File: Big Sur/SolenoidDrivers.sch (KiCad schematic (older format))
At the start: 32 parts, among them U1 DRV103H, U2 DRV103H, U3 DRV8806

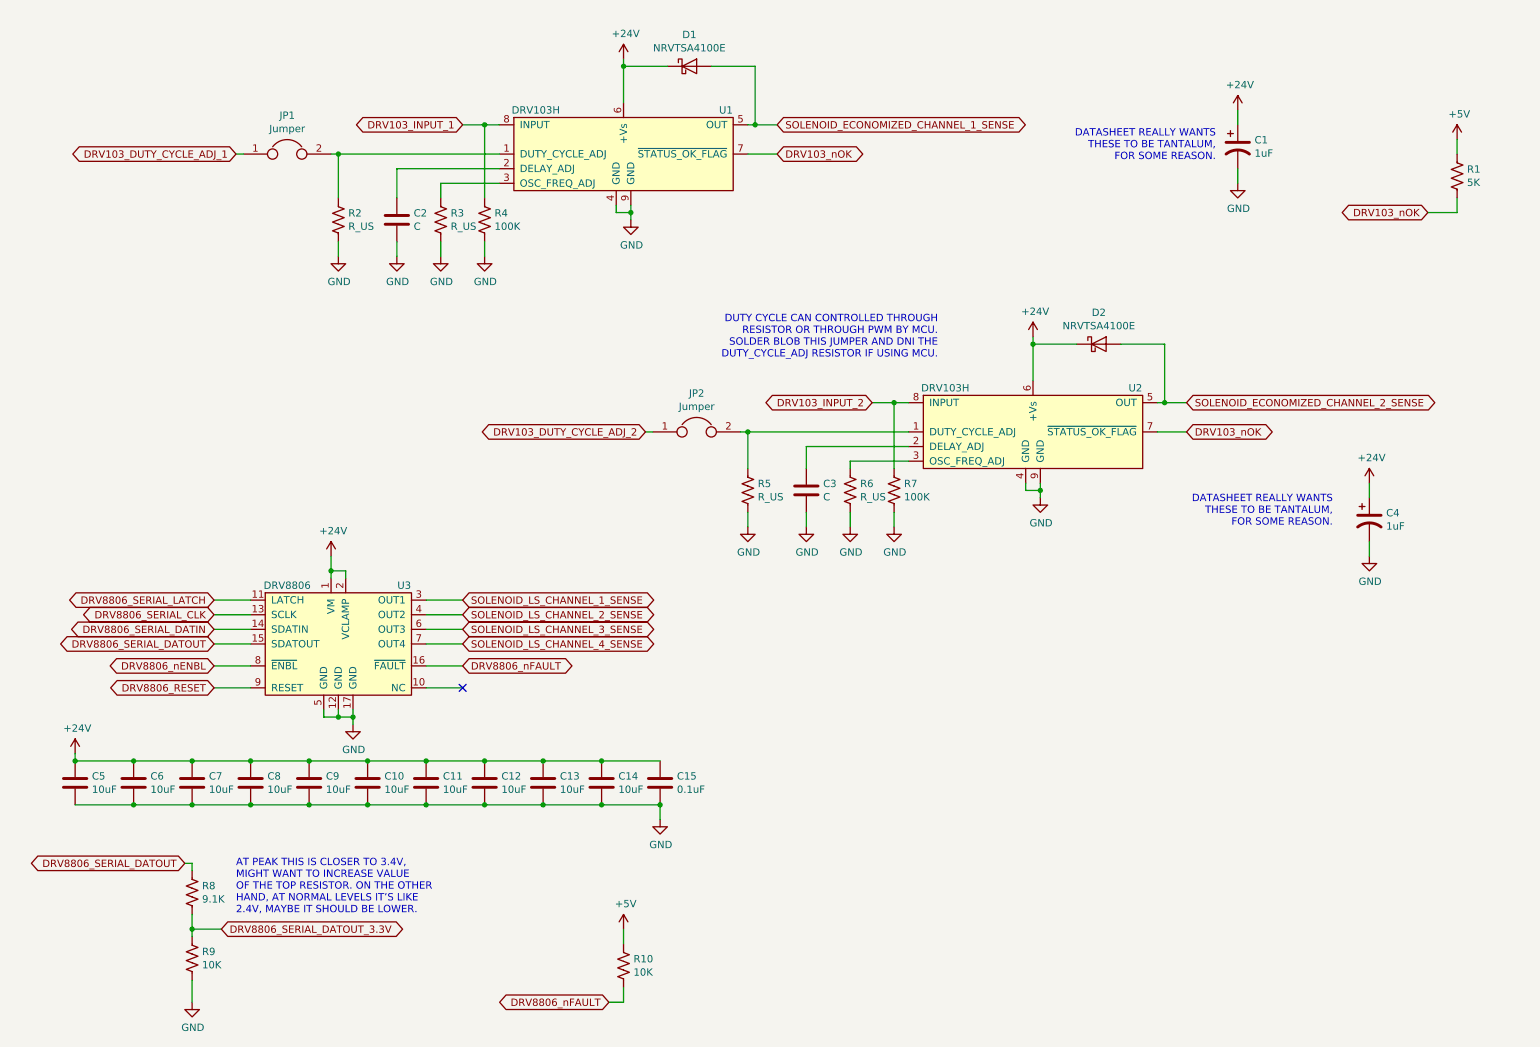
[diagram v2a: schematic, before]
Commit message: Schematics Complete
Still need to spec resistors, and XT30s, then should be ready for layout and routing.
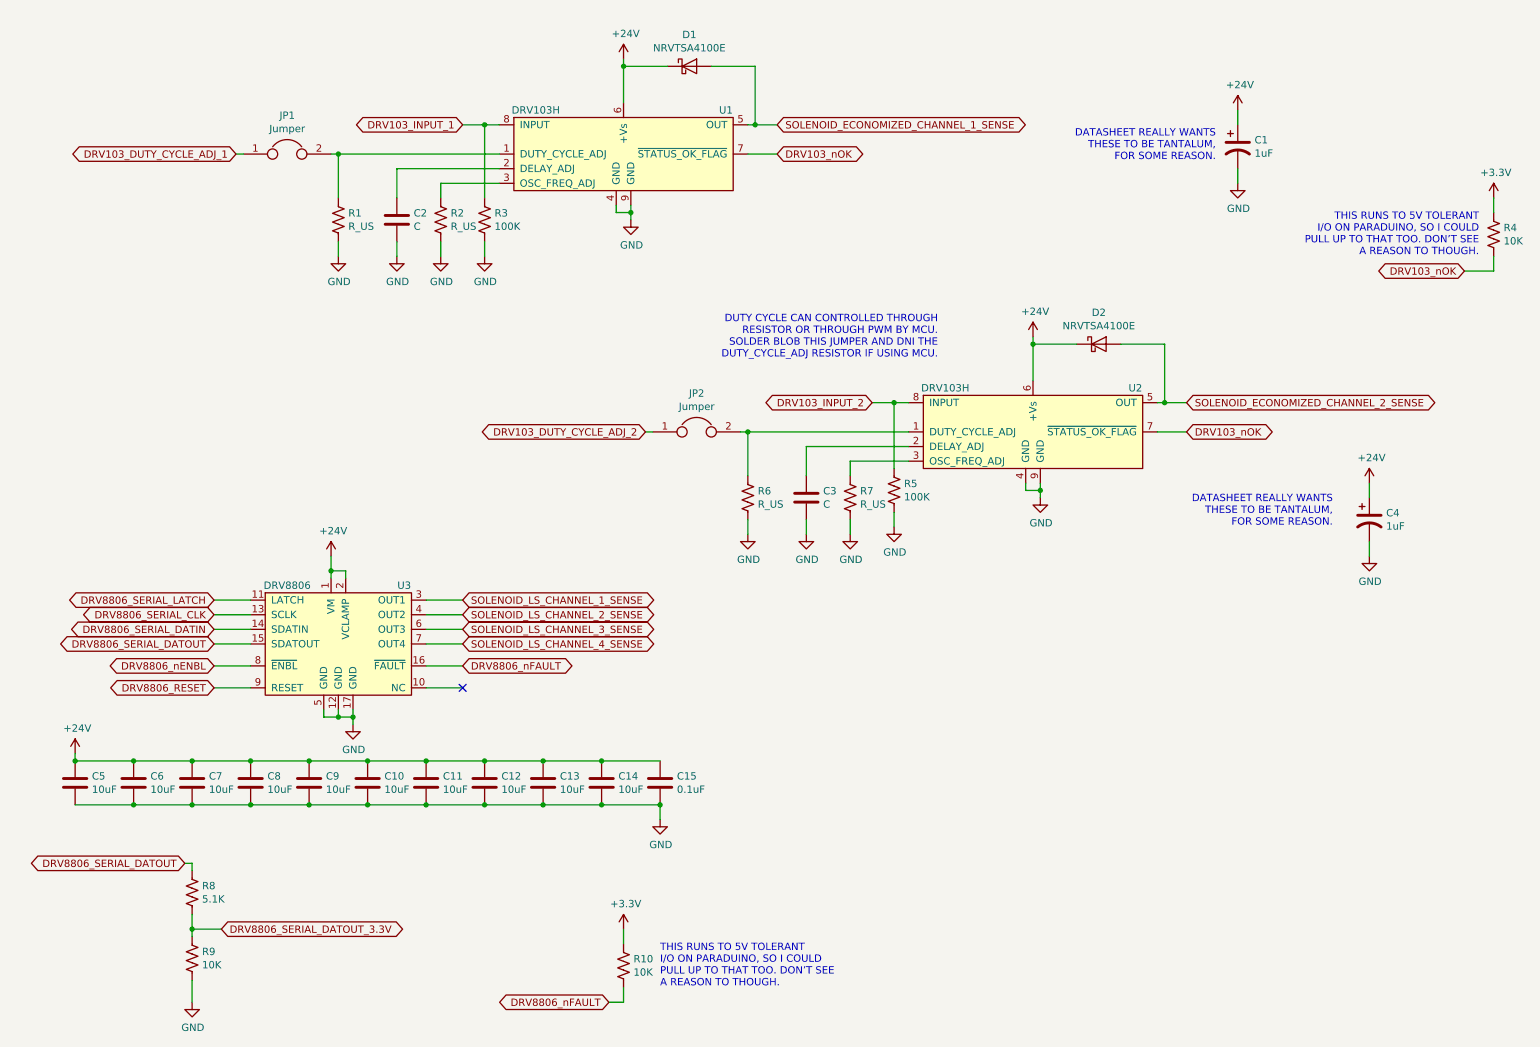
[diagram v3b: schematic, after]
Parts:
- removed R5: R_US, symbol Device:R_US
- added R7: R_US, Resistor_SMD:R_1210_3225Metric_Pad1.42x2.65mm_HandSolder, symbol Device:R_US
- C1, C4: footprint (none) -> Big Sur:KEMET_CAP_SMD_T491C105K050AT
- C2, C3: footprint (none) -> Capacitor_SMD:C_1210_3225Metric_Pad1.42x2.65mm_HandSolder
- D1, D2: footprint (none) -> Big Sur:ONSemi_SMD_Schottky_NRVTSA4100E
- JP1, JP2: footprint (none) -> Resistor_SMD:R_0805_2012Metric_Pad1.15x1.40mm_HandSolder
- R1: renamed from R2; footprint (none) -> Resistor_SMD:R_1210_3225Metric_Pad1.42x2.65mm_HandSolder
- R10, R9: footprint (none) -> Resistor_SMD:R_0603_1608Metric_Pad1.05x0.95mm_HandSolder
- R2: renamed from R3; footprint (none) -> Resistor_SMD:R_1210_3225Metric_Pad1.42x2.65mm_HandSolder
- R3: renamed from R4; footprint (none) -> Resistor_SMD:R_0603_1608Metric_Pad1.05x0.95mm_HandSolder
- R4: renamed from R1; value 5K -> 10K; footprint (none) -> Resistor_SMD:R_0603_1608Metric_Pad1.05x0.95mm_HandSolder
- R5: renamed from R7; footprint (none) -> Resistor_SMD:R_0603_1608Metric_Pad1.05x0.95mm_HandSolder
- R6: footprint (none) -> Resistor_SMD:R_1210_3225Metric_Pad1.42x2.65mm_HandSolder
- R8: value 9.1K -> 5.1K; footprint (none) -> Resistor_SMD:R_0603_1608Metric_Pad1.05x0.95mm_HandSolder
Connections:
- net GND: now also R7.2
- net at JP2.2, U2.1 (DUTY_CYCLE_ADJ): now also R6.1
- net at U2.3 (OSC_FREQ_ADJ): now also R7.1; no longer R6.1
- net +5V renamed +3V3
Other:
- note added: "THIS RUNS TO 5V TOLERANT\nI/O ON PARADUINO, SO I COULD\nPULL UP TO THAT TOO. DON’T SEE\nA REASON TO THOUGH."
- note removed: "AT PEAK THIS IS CLOSER TO 3.4V,\nMIGHT WANT TO INCREASE VALUE\nOF THE TOP RESISTOR. ON THE OTHER\nHAND, AT NORMAL LEVELS IT’S LIKE\n2.4V, MAYBE IT SHOULD BE LOWER."
- moved on the sheet: R4

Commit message: Added test points, started CAN connector.
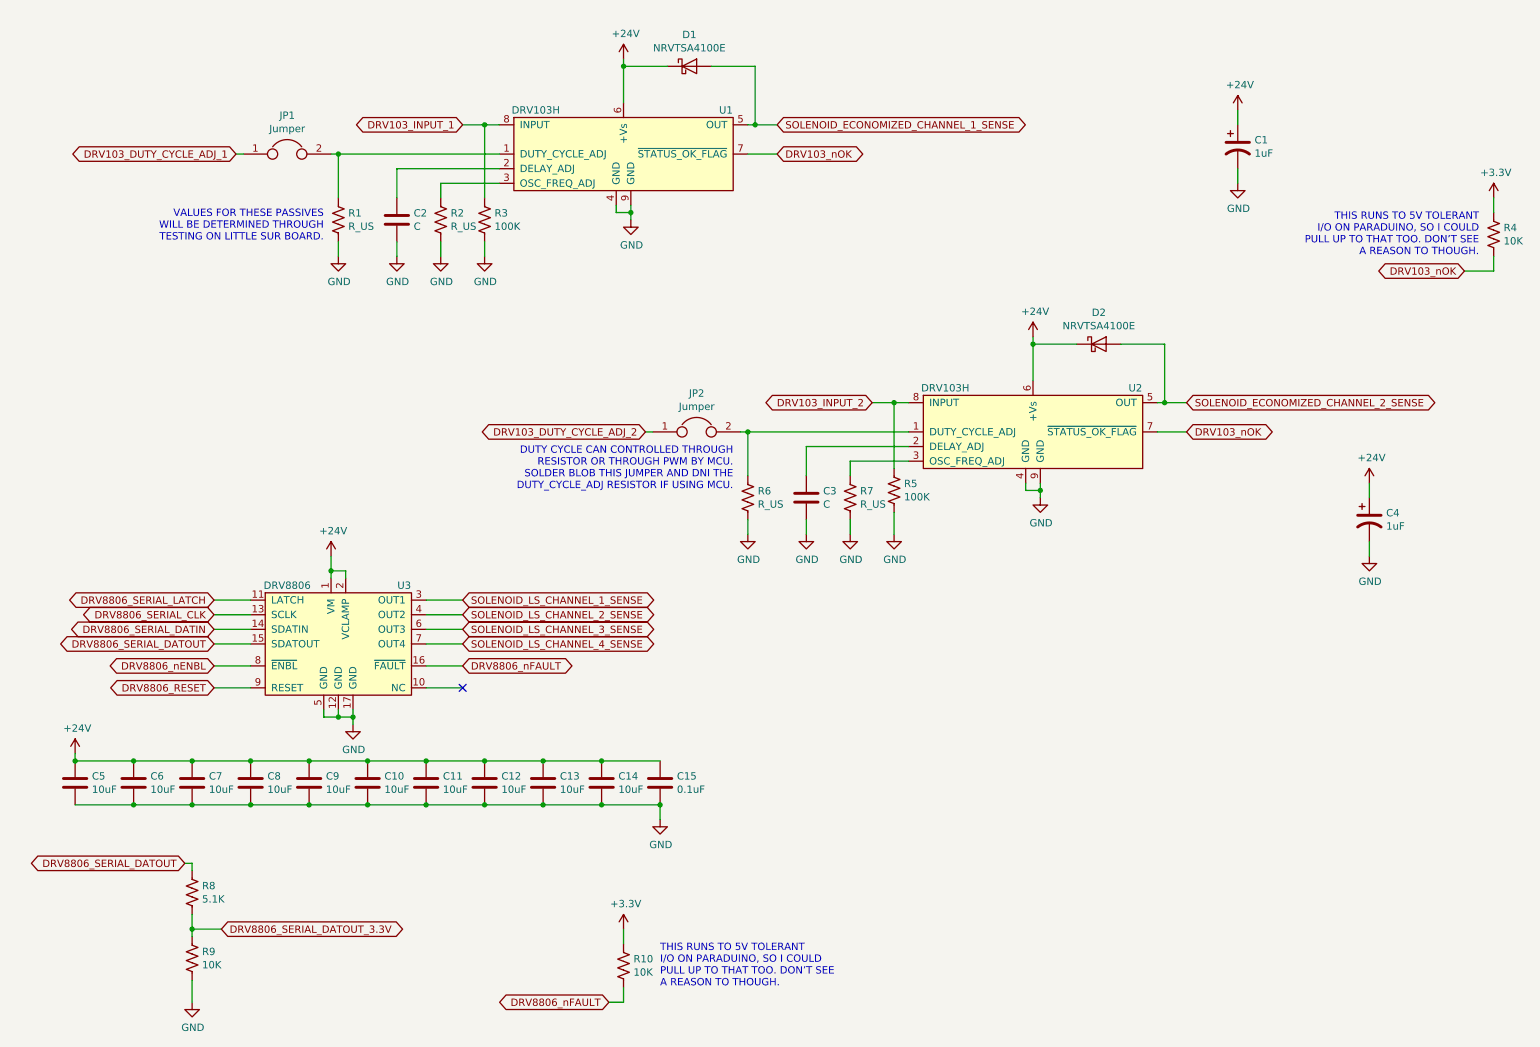
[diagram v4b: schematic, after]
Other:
- note added: "VALUES FOR THESE PASSIVES\nWILL BE DETERMINED THROUGH\nTESTING ON LITTLE SUR BOARD."
- note removed: "DATASHEET REALLY WANTS\nTHESE TO BE TANTALUM,\nFOR SOME REASON."
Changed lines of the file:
@@
 	1    0    0    -1
 $EndComp
-Text Notes 6800 3100 2    50   ~ 0
+Text Notes 5400 4000 2    50   ~ 0
 DUTY CYCLE CAN CONTROLLED THROUGH\nRESISTOR OR THROUGH PWM BY MCU.\nSOLDER BLOB THIS JUMPER AND DNI THE\nDUTY_CYCLE_ADJ RESISTOR IF USING MCU.
 Text GLabel 3550 1500 0    50   BiDi ~ 0
@@
 L power:GND #PWR?
 U 1 1 5D93927E
-P 6500 4250
+P 6500 4300
 AR Path="/5D93927E" Ref="#PWR?"  Part="1"
 AR Path="/5D6EB2B2/5D93927E" Ref="#PWR013"  Part="1"
 AR Path="/5D71C3EA/5D93927E" Ref="#PWR?"  Part="1"
 AR Path="/5D765C4F/5D93927E" Ref="#PWR?"  Part="1"
-F 0 "#PWR013" H 6500 4000 50  0001 C CNN
-F 1 "GND" H 6505 4077 50  0000 C CNN
-F 2 "" H 6500 4250 50  0001 C CNN
-F 3 "" H 6500 4250 50  0001 C CNN
-	1    6500 4250
+F 0 "#PWR013" H 6500 4050 50  0001 C CNN
+F 1 "GND" H 6505 4127 50  0000 C CNN
+F 2 "" H 6500 4300 50  0001 C CNN
+F 3 "" H 6500 4300 50  0001 C CNN
+	1    6500 4300
 	1    0    0    -1
 $EndComp
@@
 	6500 3400 6500 3850
 Wire Wire Line
-	6500 4150 6500 4250
+	6500 4150 6500 4300
 Wire Wire Line
 	3300 4750 3550 4750
@@
 	1    0    0    -1
 $EndComp
-Text Notes 8700 1750 2    50   ~ 0
-DATASHEET REALLY WANTS\nTHESE TO BE TANTALUM,\nFOR SOME REASON.
 Text GLabel 1850 5050 0    50   BiDi ~ 0
 DRV8806_SERIAL_DATOUT
 Wire Wire Line
 	1850 5050 2100 5050
-Text Notes 9500 4250 2    50   ~ 0
-DATASHEET REALLY WANTS\nTHESE TO BE TANTALUM,\nFOR SOME REASON.
 Wire Wire Line
 	900  5850 1300 5850
@@
 	1    0    0    -1
 $EndComp
+Text Notes 2600 2300 2    50   ~ 0
+VALUES FOR THESE PASSIVES\nWILL BE DETERMINED THROUGH\nTESTING ON LITTLE SUR BOARD.
 $EndSCHEMATC
